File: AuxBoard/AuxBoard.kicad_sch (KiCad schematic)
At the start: 16 parts, among them J1 ATX-24, J10 MatBIn, J2 RPI4B, J3 Passthrough, J4 MatrixASupply, J5 MatrixBSupply, J6 BigLED, J7 MatAOut, J8 MatAIn, J9 MatBOut, SW1 SW_DPST, U1 74125

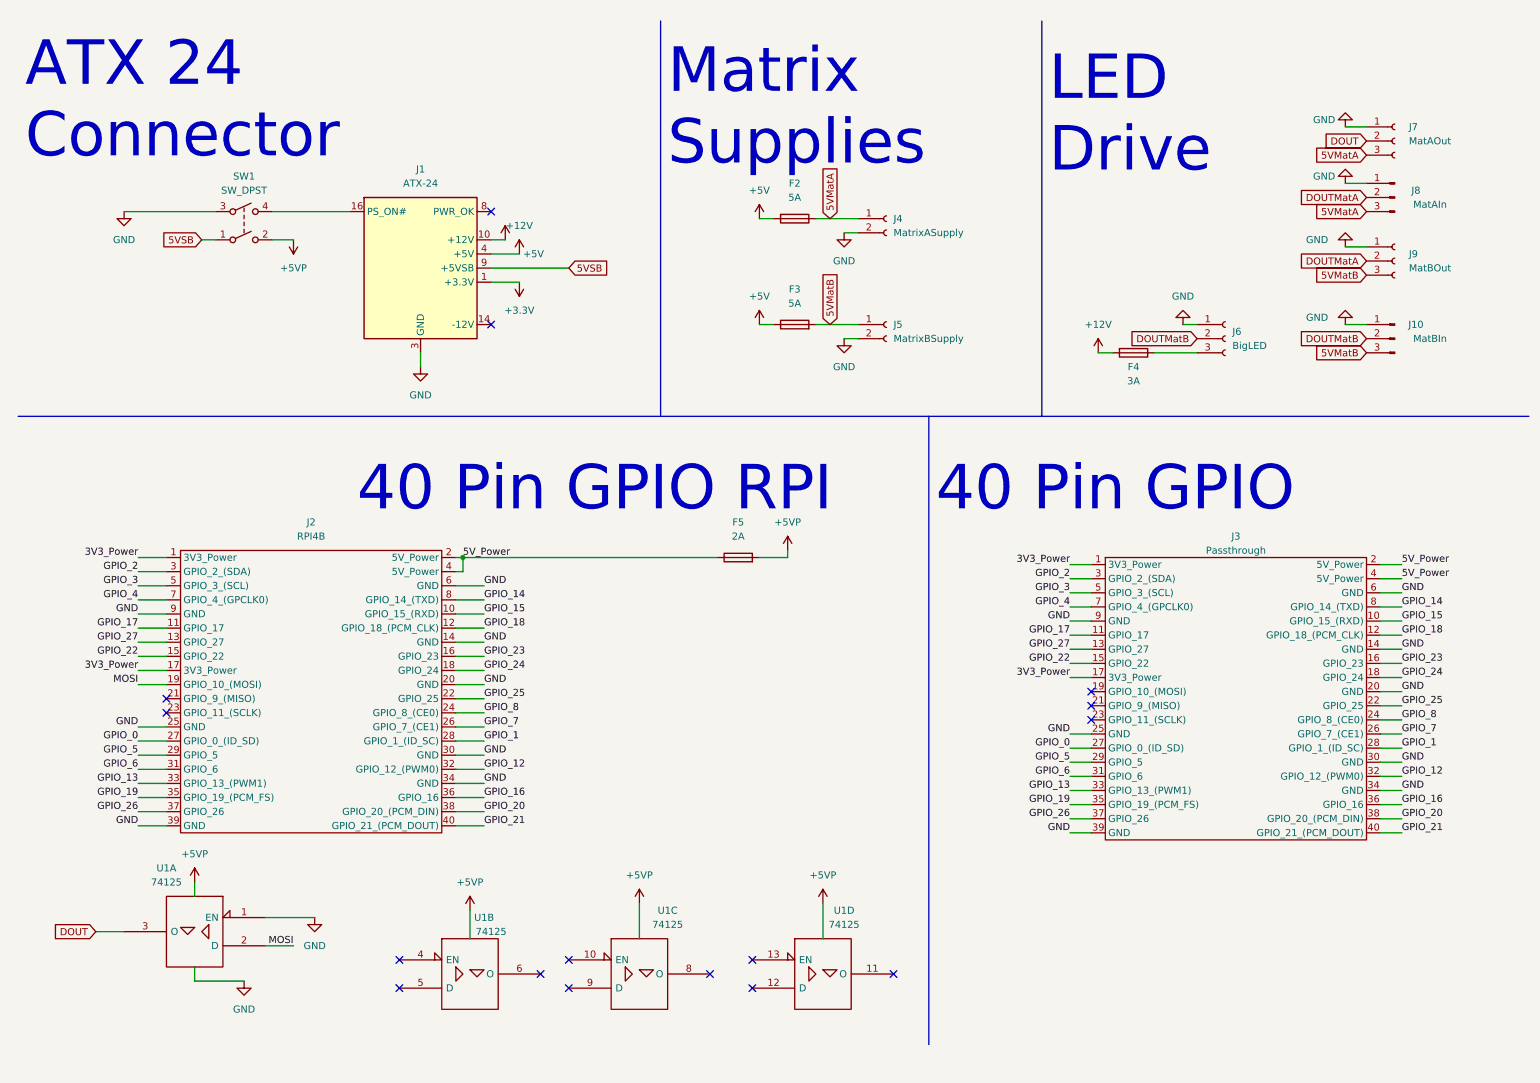
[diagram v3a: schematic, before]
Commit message: Draft Schematic Finished. Added ZVD and Changed to polyfuses
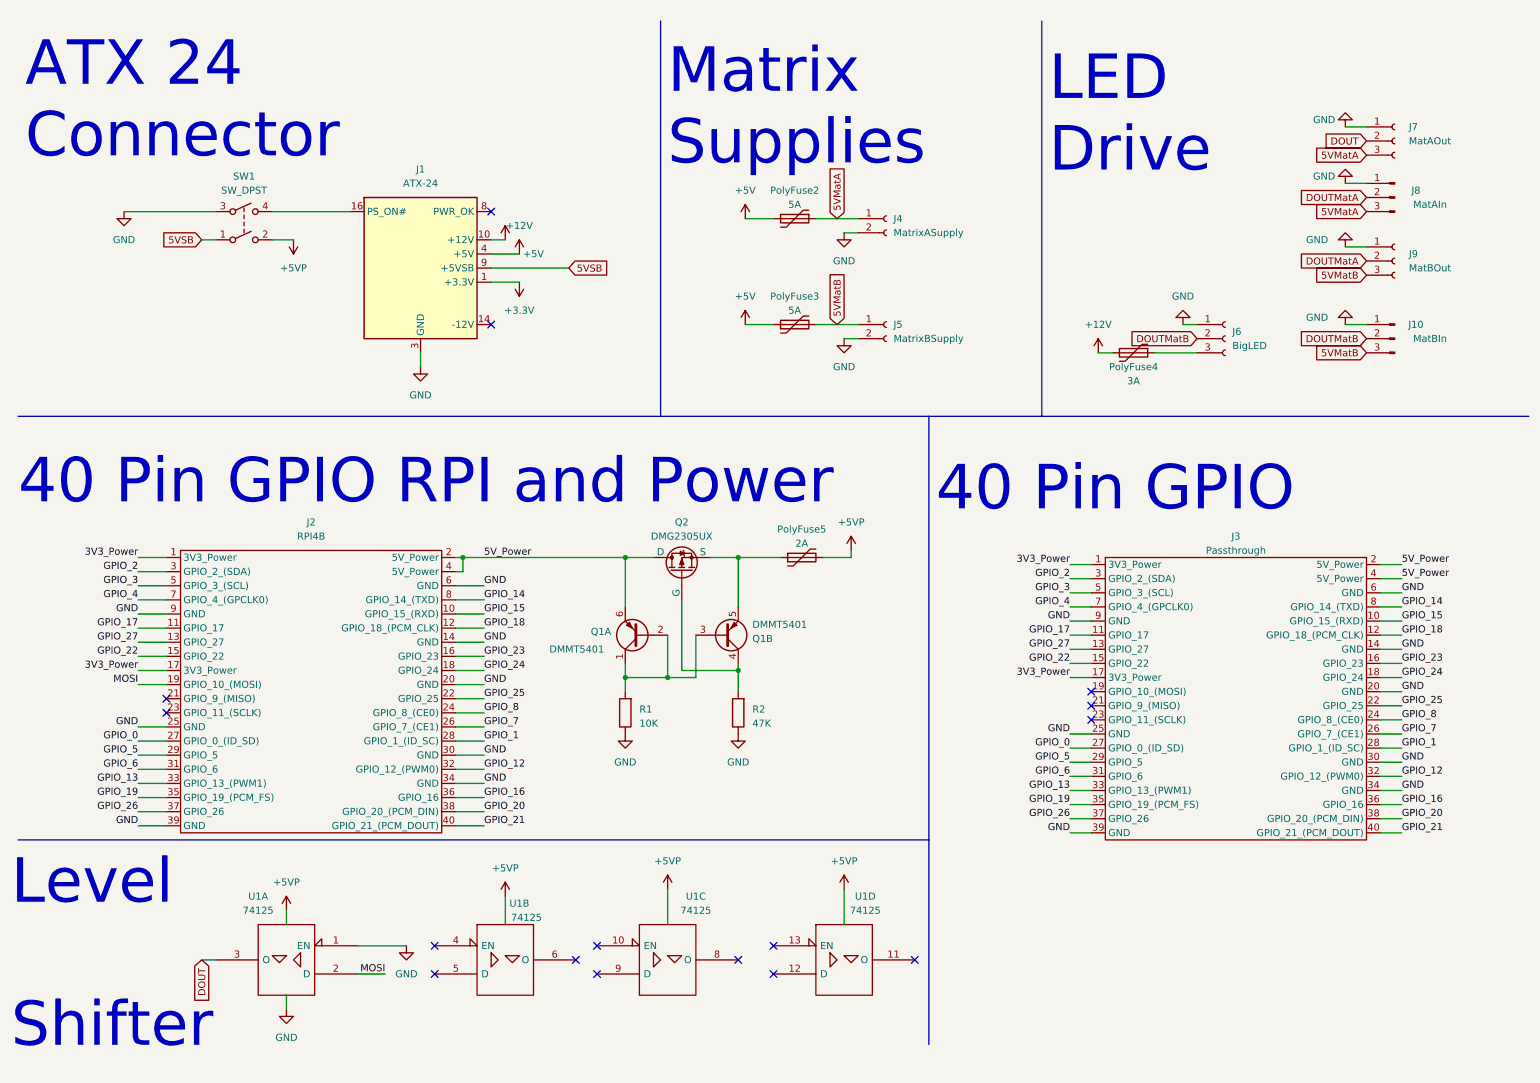
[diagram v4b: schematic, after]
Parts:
- added Q1: DMMT5401, symbol Device:Q_Dual_PNP_PNP_C1B1B2C2E2E1
- added Q2: DMG2305UX, symbol Simulation_SPICE:PMOS
- added R1: 10K, symbol Device:R
- added R2: 47K, symbol Device:R
- PolyFuse2: renamed from F2; symbol Device:Fuse -> Device:Polyfuse
- PolyFuse3: renamed from F3; symbol Device:Fuse -> Device:Polyfuse
- PolyFuse4: renamed from F4; symbol Device:Fuse -> Device:Polyfuse
- PolyFuse5: renamed from F5; symbol Device:Fuse -> Device:Polyfuse
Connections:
- net 5V_Power: now also Q1.6 (E1), Q2.1 (D); no longer PolyFuse5.1
- net GND: now also R1.1, R2.1
- new net: Q1.1 (C1), Q1.2 (B1), Q1.3 (B2), R1.2
- new net: Q1.4 (C2), Q2.2 (G), R2.2
- new net: PolyFuse5.1, Q1.5 (E2), Q2.3 (S)
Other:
- note added: "40 Pin GPIO RPI and Power"
- note added: "Level Shifter"
- note removed: "40 Pin GPIO RPI"
- moved on the sheet: U1A, U1B, U1C, U1D

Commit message: Added fan header and mosfet control for PI power supply
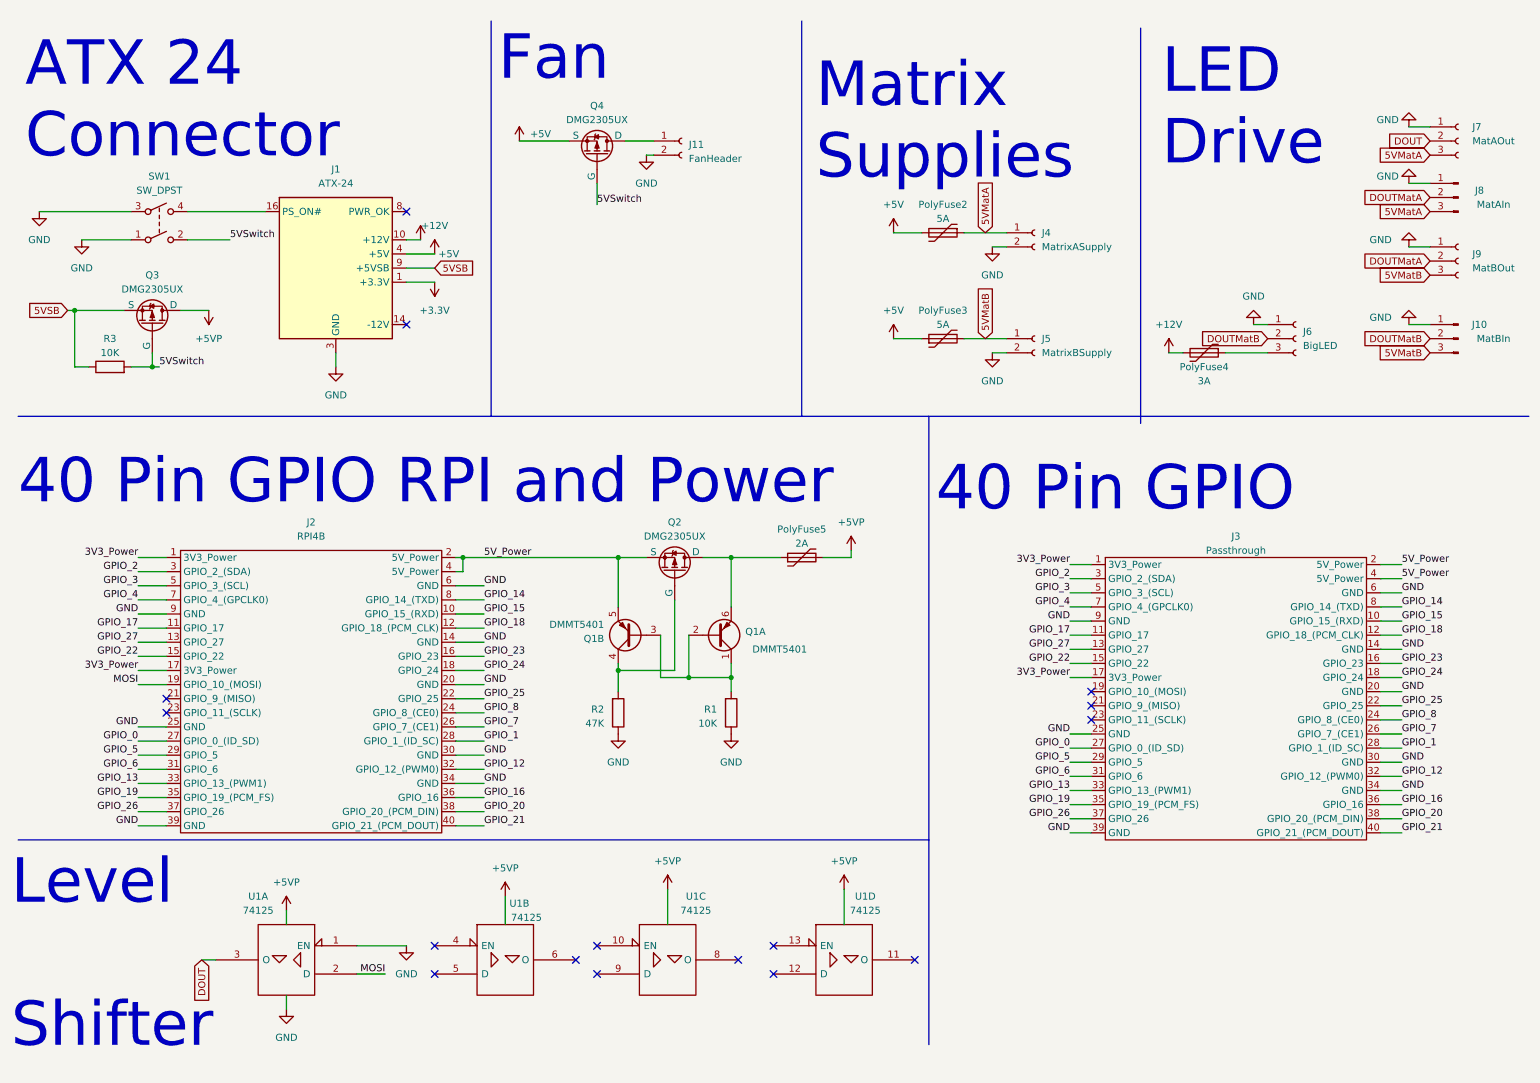
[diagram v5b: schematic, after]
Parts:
- added J11: FanHeader, Connector_PinSocket_2.54mm:PinSocket_1x02_P2.54mm_Vertical, symbol Connector:Conn_01x02_Female
- added Q3, Q4: DMG2305UX, symbol Simulation_SPICE:PMOS
- added R3: 10K, symbol Device:R
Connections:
- net +5V: now also Q4.3 (S)
- net +5VP: now also Q3.1 (D); no longer SW1.2
- net 5VSB: now also Q3.3 (S), R3.1; no longer SW1.1
- net 5V_Power: now also Q1.5 (E2), Q2.3 (S); no longer Q1.6 (E1), Q2.1 (D)
- net GND: now also SW1.1, J11.2 (Pin_2)
- new net: PolyFuse5.1, Q1.6 (E1), Q2.1 (D)
- new net: J11.1 (Pin_1), Q4.1 (D)
- new net 5VSwitch: Q3.2 (G), Q4.2 (G), R3.2, SW1.2
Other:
- note added: "Fan"
- moved on the sheet: J1, J10, J4, J5, J6, J7, J8, J9, PolyFuse2, PolyFuse3, PolyFuse4, Q1A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

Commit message: Simulated Ideal Diode to check functionality. Swaped Tristate buffer for hex inverter. Swapped to passthrough footprint.
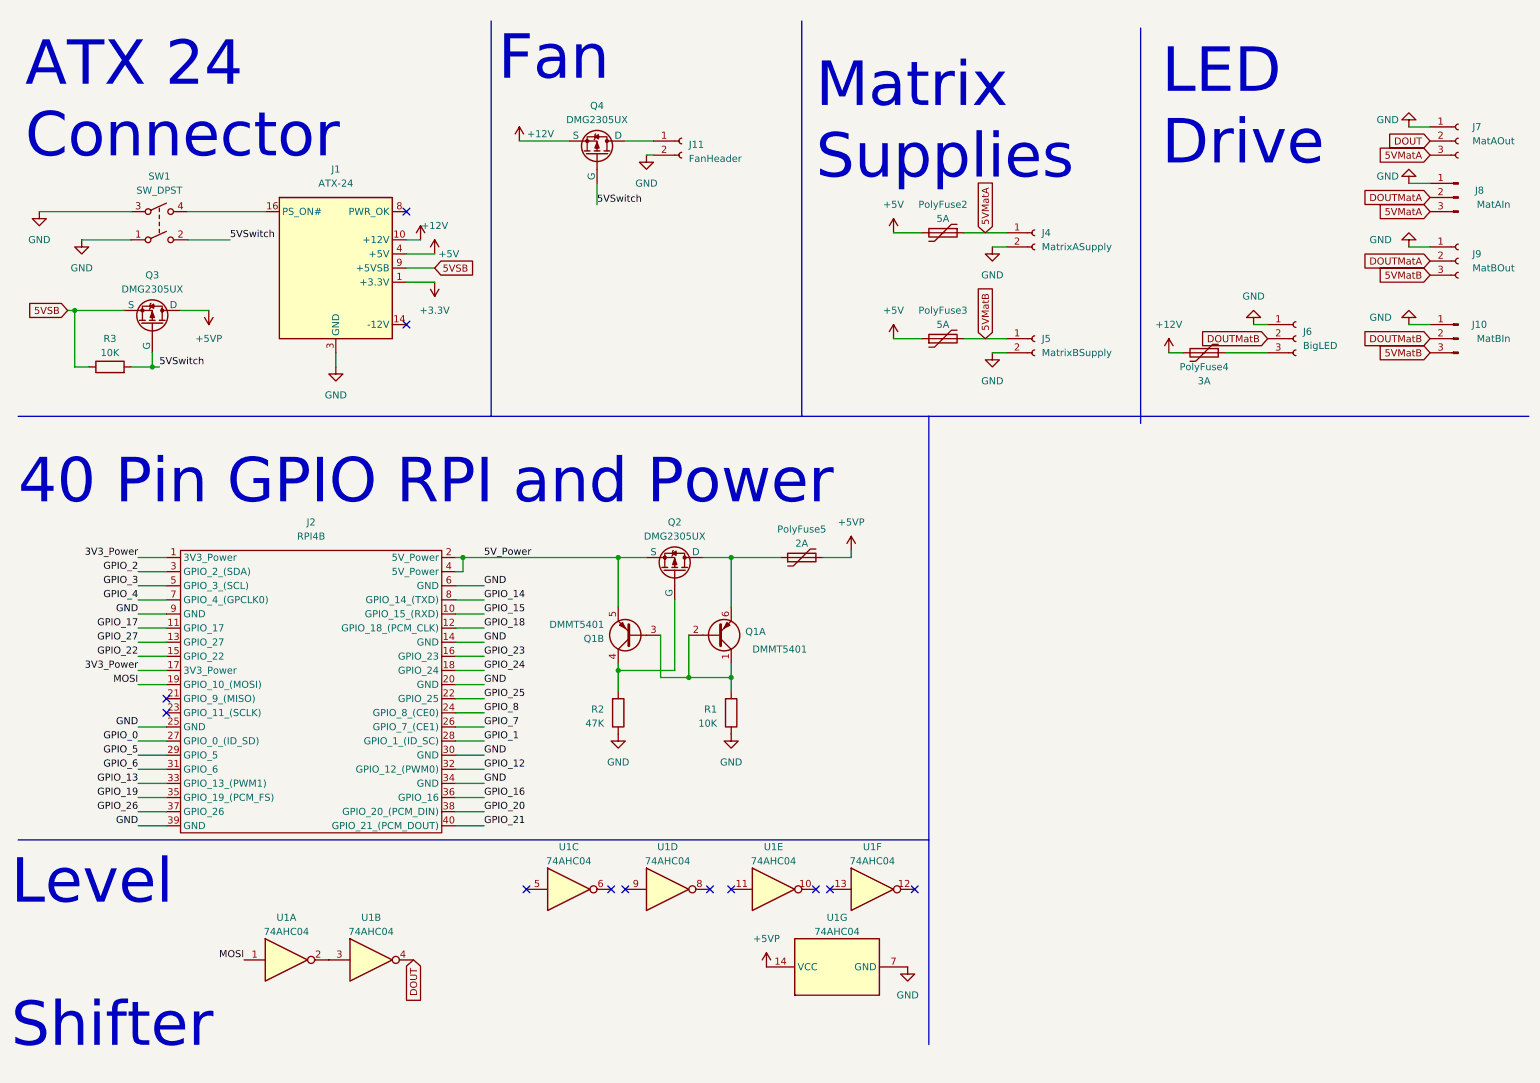
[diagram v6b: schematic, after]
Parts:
- removed J3: Passthrough, Connector_PinSocket_2.54mm:PinSocket_2x20_P2.54mm_FLIPED_Vertical_SMD, symbol Tom's Parts:RPI4B
- removed U1: 74125, Package_DIP:DIP-14_W7.62mm_LongPads, symbol 74xx_IEEE:74125
- added U1: 74AHC04, Package_DIP:DIP-14_W7.62mm, symbol 74xx:74AHC04
- J2: footprint Connector_PinSocket_2.54mm:PinSocket_2x20_P2.54mm_Vertical_SMD -> Tom's Parts:PI Header Passthrough
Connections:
- net +5VP: now also U1.14 (VCC)
- net DOUT: now also U1.4
- net GND: now also U1.7 (GND)
- net MOSI: now also U1.1
- new net: U1.2, U1.3
- no-connect marks 16 -> 12
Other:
- note removed: "40 Pin GPIO"

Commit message: Final PCB Layout
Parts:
- added H1, H2, H3, H4, H5, H6: MountingHole, Tom's Parts:MountingHole_2.75mm_RPI_HAT, symbol Mechanical:MountingHole
- PolyFuse2, PolyFuse3, PolyFuse4: footprint (none) -> Fuse:Fuse_2920_7451Metric_Pad2.10x5.45mm_HandSolder
- PolyFuse5: footprint (none) -> Fuse:Fuse_1812_4532Metric_Pad1.30x3.40mm_HandSolder
- Q1: footprint (none) -> Package_TO_SOT_SMD:SOT-23-6
- Q2, Q3, Q4: footprint (none) -> Package_TO_SOT_SMD:SOT-23-3
- R1, R2, R3: footprint (none) -> Resistor_SMD:R_0805_2012Metric_Pad1.20x1.40mm_HandSolder
- SW1: footprint (none) -> Connector_PinHeader_2.54mm:PinHeader_2x02_P2.54mm_Vertical
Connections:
- net +12V: now also Q4.3 (S)
- net +5V: no longer Q4.3 (S)
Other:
- moved on the sheet: U1G
